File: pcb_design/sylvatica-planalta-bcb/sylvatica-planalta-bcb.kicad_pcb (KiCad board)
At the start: 2 copper layers, 93 x 93 mm, 5 parts, among them J1 USB_C_Receptacle, J2 Conn_02x07_Odd_Even, J3 USB_C_Receptacle, J4 Conn_01x06

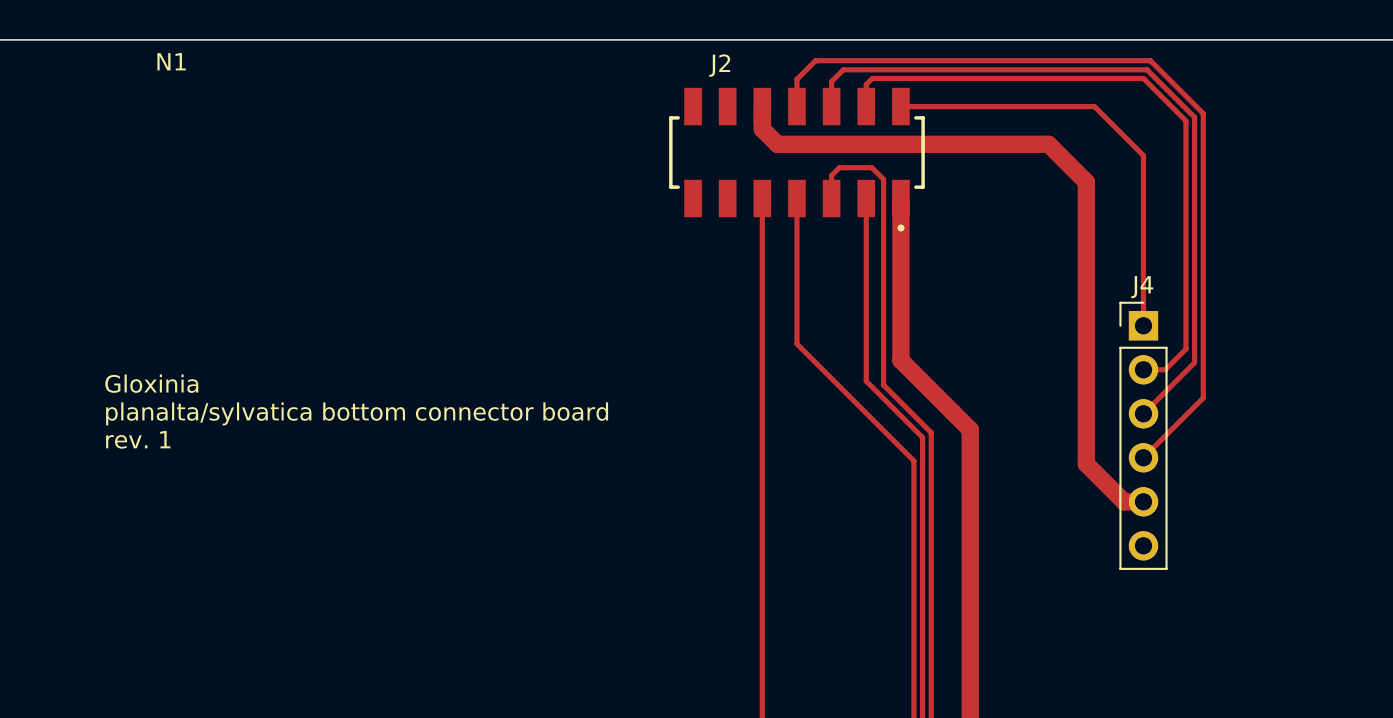
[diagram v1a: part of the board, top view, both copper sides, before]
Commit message: Expose RTCC pin for synchronisation
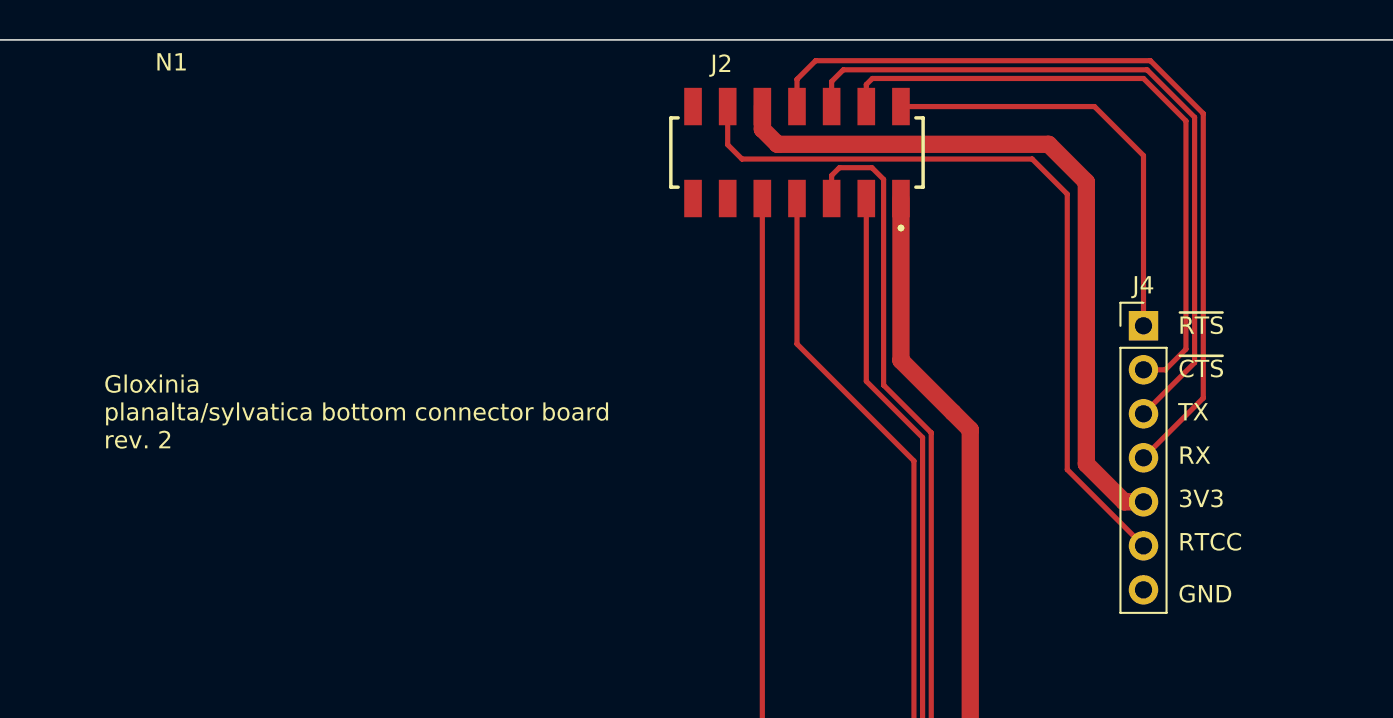
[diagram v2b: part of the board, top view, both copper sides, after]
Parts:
- J4: value Conn_01x06 -> Conn_01x07; footprint Connector_PinHeader_2.54mm:PinHeader_1x06_P2.54mm_Vertical -> Connector_PinHeader_2.54mm:PinHeader_1x07_P2.54mm_Vertical
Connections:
- J2 pad 12: GND -> /RTCC
- J4 pad 6: GND -> /RTCC
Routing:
- net /RTCC: track 0.00 -> 45.1 mm
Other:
- board text added: "3V3"
- board text added: "GND"
- board text added: "Gloxinia planalta/sylvatica bottom connector board rev. 2"
- board text added: "RTCC"
- board text added: "RX"
- board text added: "TX"
- board text added: "~{CTS}"
- board text added: "~{RTS}"
- board text removed: "Gloxinia planalta/sylvatica bottom connector board rev. 1"
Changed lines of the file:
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@@
   (net 30 "unconnected-(J3-PadB10)")
   (net 31 "unconnected-(J3-PadB11)")
+  (net 32 "/RTCC")
   (footprint "custom_footprints:Enclosure-Gloxinia4" (layer "F.Cu")
     (at 85 85)
@@
       (net 1 "GND") (pinfunction "Pin_11") (pintype "passive"))
     (pad "12" smd rect (at -4 -2.654) (size 1.02 2.16) (layers "F.Cu" "F.Paste" "F.Mask")
-      (net 1 "GND") (pinfunction "Pin_12") (pintype "passive"))
+      (net 32 "/RTCC") (pinfunction "Pin_12") (pintype "passive"))
     (pad "13" smd rect (at -6 2.654) (size 1.02 2.16) (layers "F.Cu" "F.Paste" "F.Mask")
       (net 1 "GND") (pinfunction "Pin_13") (pintype "passive"))
     (pad "14" smd rect (at -6 -2.654) (size 1.02 2.16) (layers "F.Cu" "F.Paste" "F.Mask")
       (net 1 "GND") (pinfunction "Pin_14") (pintype "passive"))
+  )
+  (footprint "Connector_PinHeader_2.54mm:PinHeader_1x07_P2.54mm_Vertical" (layer "F.Cu")
+    (at 105 55)
+    (descr "Through hole straight pin header, 1x07, 2.54mm pitch, single row")
+    (tags "Through hole pin header THT 1x07 2.54mm single row")
+    (property "Sheetfile" "sylvatica-planalta-bcb.kicad_sch")
+    (property "Sheetname" "")
+    (attr through_hole)
+    (fp_text reference "J4" (at 0 -2.33) (layer "F.SilkS")
+      (effects (font (size 1 1) (thickness 0.15)))
+    )
+    (fp_text value "Conn_01x07" (at 0 17.57) (layer "F.Fab")
+      (effects (font (size 1 1) (thickness 0.15)))
+    )
+    (fp_text user "${REFERENCE}" (at 0 7.62 90) (layer "F.Fab")
+      (effects (font (size 1 1) (thickness 0.15)))
+    )
+    (fp_line (start -1.33 1.27) (end -1.33 16.57) (layer "F.SilkS") (width 0.12))
+    (fp_line (start -1.33 1.27) (end 1.33 1.27) (layer "F.SilkS") (width 0.12))
+    (fp_line (start 1.33 1.27) (end 1.33 16.57) (layer "F.SilkS") (width 0.12))
+    (fp_line (start -1.33 -1.33) (end 0 -1.33) (layer "F.SilkS") (width 0.12))
+    (fp_line (start -1.33 0) (end -1.33 -1.33) (layer "F.SilkS") (width 0.12))
+    (fp_line (start -1.33 16.57) (end 1.33 16.57) (layer "F.SilkS") (width 0.12))
+    (fp_line (start 1.8 17.05) (end 1.8 -1.8) (layer "F.CrtYd") (width 0.05))
+    (fp_line (start -1.8 -1.8) (end -1.8 17.05) (layer "F.CrtYd") (width 0.05))
+    (fp_line (start 1.8 -1.8) (end -1.8 -1.8) (layer "F.CrtYd") (width 0.05))
+    (fp_line (start -1.8 17.05) (end 1.8 17.05) (layer "F.CrtYd") (width 0.05))
+    (fp_line (start 1.27 16.51) (end -1.27 16.51) (layer "F.Fab") (width 0.1))
+    (fp_line (start -1.27 -0.635) (end -0.635 -1.27) (layer "F.Fab") (width 0.1))
+    (fp_line (start -0.635 -1.27) (end 1.27 -1.27) (layer "F.Fab") (width 0.1))
+    (fp_line (start -1.27 16.51) (end -1.27 -0.635) (layer "F.Fab") (width 0.1))
+    (fp_line (start 1.27 -1.27) (end 1.27 16.51) (layer "F.Fab") (width 0.1))
+    (pad "1" thru_hole rect (at 0 0) (size 1.7 1.7) (drill 1) (layers *.Cu *.Mask)
+      (net 17 "/~{RTS}") (pinfunction "Pin_1") (pintype "passive"))
+    (pad "2" thru_hole oval (at 0 2.54) (size 1.7 1.7) (drill 1) (layers *.Cu *.Mask)
+      (net 18 "/~{CTS}") (pinfunction "Pin_2") (pintype "passive"))
+    (pad "3" thru_hole oval (at 0 5.08) (size 1.7 1.7) (drill 1) (layers *.Cu *.Mask)
+      (net 19 "/TX") (pinfunction "Pin_3") (pintype "passive"))
+    (pad "4" thru_hole oval (at 0 7.62) (size 1.7 1.7) (drill 1) (layers *.Cu *.Mask)
+      (net 20 "/RX") (pinfunction "Pin_4") (pintype "passive"))
+    (pad "5" thru_hole oval (at 0 10.16) (size 1.7 1.7) (drill 1) (layers *.Cu *.Mask)
+      (net 21 "+3.3V") (pinfunction "Pin_5") (pintype "passive"))
+    (pad "6" thru_hole oval (at 0 12.7) (size 1.7 1.7) (drill 1) (layers *.Cu *.Mask)
+      (net 32 "/RTCC") (pinfunction "Pin_6") (pintype "passive"))
+    (pad "7" thru_hole oval (at 0 15.24) (size 1.7 1.7) (drill 1) (layers *.Cu *.Mask)
+      (net 1 "GND") (pinfunction "Pin_7") (pintype "passive"))
+    (model "${KICAD6_3DMODEL_DIR}/Connector_PinHeader_2.54mm.3dshapes/PinHeader_1x07_P2.54mm_Vertical.wrl"
+      (offset (xyz 0 0 0))
+      (scale (xyz 1 1 1))
+      (rotate (xyz 0 0 0))
+    )
   )
   (footprint "custom_footprints:USB_C_Receptacle_Amphenol_12401861XX12A" (layer "F.Cu")
@@
     )
   )
-  (footprint "Connector_PinHeader_2.54mm:PinHeader_1x06_P2.54mm_Vertical" (layer "F.Cu")
-    (at 105 55)
-    (descr "Through hole straight pin header, 1x06, 2.54mm pitch, single row")
-    (tags "Through hole pin header THT 1x06 2.54mm single row")
-    (property "Sheetfile" "sylvatica-planalta-bcb.kicad_sch")
-    (property "Sheetname" "")
-    (attr through_hole)
-    (fp_text reference "J4" (at 0 -2.33) (layer "F.SilkS")
-      (effects (font (size 1 1) (thickness 0.15)))
-    )
-    (fp_text value "Conn_01x06" (at 0 15.03) (layer "F.Fab")
-      (effects (font (size 1 1) (thickness 0.15)))
-    )
-    (fp_text user "${REFERENCE}" (at 0 6.35 90) (layer "F.Fab")
-      (effects (font (size 1 1) (thickness 0.15)))
-    )
-    (fp_line (start -1.33 0) (end -1.33 -1.33) (layer "F.SilkS") (width 0.12))
-    (fp_line (start -1.33 1.27) (end 1.33 1.27) (layer "F.SilkS") (width 0.12))
-    (fp_line (start -1.33 1.27) (end -1.33 14.03) (layer "F.SilkS") (width 0.12))
-    (fp_line (start 1.33 1.27) (end 1.33 14.03) (layer "F.SilkS") (width 0.12))
-    (fp_line (start -1.33 -1.33) (end 0 -1.33) (layer "F.SilkS") (width 0.12))
-    (fp_line (start -1.33 14.03) (end 1.33 14.03) (layer "F.SilkS") (width 0.12))
-    (fp_line (start -1.8 -1.8) (end -1.8 14.5) (layer "F.CrtYd") (width 0.05))
-    (fp_line (start 1.8 -1.8) (end -1.8 -1.8) (layer "F.CrtYd") (width 0.05))
-    (fp_line (start -1.8 14.5) (end 1.8 14.5) (layer "F.CrtYd") (width 0.05))
-    (fp_line (start 1.8 14.5) (end 1.8 -1.8) (layer "F.CrtYd") (width 0.05))
-    (fp_line (start -1.27 13.97) (end -1.27 -0.635) (layer "F.Fab") (width 0.1))
-    (fp_line (start 1.27 -1.27) (end 1.27 13.97) (layer "F.Fab") (width 0.1))
-    (fp_line (start 1.27 13.97) (end -1.27 13.97) (layer "F.Fab") (width 0.1))
-    (fp_line (start -1.27 -0.635) (end -0.635 -1.27) (layer "F.Fab") (width 0.1))
-    (fp_line (start -0.635 -1.27) (end 1.27 -1.27) (layer "F.Fab") (width 0.1))
-    (pad "1" thru_hole rect (at 0 0) (size 1.7 1.7) (drill 1) (layers *.Cu *.Mask)
-      (net 17 "/~{RTS}") (pinfunction "Pin_1") (pintype "passive"))
-    (pad "2" thru_hole oval (at 0 2.54) (size 1.7 1.7) (drill 1) (layers *.Cu *.Mask)
-      (net 18 "/~{CTS}") (pinfunction "Pin_2") (pintype "passive"))
-    (pad "3" thru_hole oval (at 0 5.08) (size 1.7 1.7) (drill 1) (layers *.Cu *.Mask)
-      (net 19 "/TX") (pinfunction "Pin_3") (pintype "passive"))
-    (pad "4" thru_hole oval (at 0 7.62) (size 1.7 1.7) (drill 1) (layers *.Cu *.Mask)
-      (net 20 "/RX") (pinfunction "Pin_4") (pintype "passive"))
-    (pad "5" thru_hole oval (at 0 10.16) (size 1.7 1.7) (drill 1) (layers *.Cu *.Mask)
-      (net 21 "+3.3V") (pinfunction "Pin_5") (pintype "passive"))
-    (pad "6" thru_hole oval (at 0 12.7) (size 1.7 1.7) (drill 1) (layers *.Cu *.Mask)
-      (net 1 "GND") (pinfunction "Pin_6") (pintype "passive"))
-    (model "${KICAD6_3DMODEL_DIR}/Connector_PinHeader_2.54mm.3dshapes/PinHeader_1x06_P2.54mm_Vertical.wrl"
-      (offset (xyz 0 0 0))
-      (scale (xyz 1 1 1))
-      (rotate (xyz 0 0 0))
-    )
-  )
   (footprint "custom_footprints:USB_C_Receptacle_Amphenol_12401861XX12A" (layer "F.Cu")
     (at 107.5 127.9)
@@
   (gr_line (start 38.5 131.5) (end 38.5 38.5) (layer "Edge.Cuts") (width 0.1))
   (gr_line (start 131.5 131.5) (end 38.5 131.5) (layer "Edge.Cuts") (width 0.1))
-  (gr_text "Gloxinia\nplanalta/sylvatica bottom connector board\nrev. 1" (at 45 60) (layer "F.SilkS")
+  (gr_text "~{CTS}" (at 107 57.5) (layer "F.SilkS")
+    (effects (font (size 1 1) (thickness 0.15)) (justify left))
+  )
+  (gr_text "Gloxinia\nplanalta/sylvatica bottom connector board\nrev. 2" (at 45 60) (layer "F.SilkS")
+    (effects (font (size 1 1) (thickness 0.15)) (justify left))
+  )
+  (gr_text "~{RTS}" (at 107 55) (layer "F.SilkS")
+    (effects (font (size 1 1) (thickness 0.15)) (justify left))
+  )
+  (gr_text "TX" (at 107 60) (layer "F.SilkS")
+    (effects (font (size 1 1) (thickness 0.15)) (justify left))
+  )
+  (gr_text "RX" (at 107 62.5) (layer "F.SilkS")
+    (effects (font (size 1 1) (thickness 0.15)) (justify left))
+  )
+  (gr_text "RTCC" (at 107 67.5) (layer "F.SilkS")
+    (effects (font (size 1 1) (thickness 0.15)) (justify left))
+  )
+  (gr_text "3V3" (at 107 65) (layer "F.SilkS")
+    (effects (font (size 1 1) (thickness 0.15)) (justify left))
+  )
+  (gr_text "GND" (at 107 70.5) (layer "F.SilkS")
     (effects (font (size 1 1) (thickness 0.15)) (justify left))
   )
@@
   (segment (start 101.7 62.975) (end 101.7 46.7) (width 1) (layer "F.Cu") (net 21))
   (segment (start 105 65.16) (end 103.885 65.16) (width 1) (layer "F.Cu") (net 21))
+  (segment (start 98.575 45.375) (end 81.825 45.375) (width 0.3) (layer "F.Cu") (net 32))
+  (segment (start 81 44.55) (end 81 42.346) (width 0.3) (layer "F.Cu") (net 32))
+  (segment (start 100.6 47.4) (end 98.575 45.375) (width 0.3) (layer "F.Cu") (net 32))
+  (segment (start 81.825 45.375) (end 81 44.55) (width 0.3) (layer "F.Cu") (net 32))
+  (segment (start 105 67.7) (end 100.6 63.3) (width 0.3) (layer "F.Cu") (net 32))
+  (segment (start 100.6 63.3) (end 100.6 47.4) (width 0.3) (layer "F.Cu") (net 32))
   (zone (net 1) (net_name "GND") (layer "F.Cu") (hatch edge 0.508)
     (connect_pads (clearance 0.508))
